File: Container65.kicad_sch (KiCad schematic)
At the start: 25 parts

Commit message: Matrix created
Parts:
- removed C? (x9): 100n, Capacitor_SMD:C_0603_1608Metric, symbol Device:C
- removed C? (x2): 1u, Capacitor_SMD:C_0603_1608Metric, symbol Device:C
- removed C? (x2): 10u, Capacitor_SMD:C_0603_1608Metric, symbol Device:C
- removed C? (x2): 15pf, Capacitor_SMD:C_0603_1608Metric, symbol Device:C
- removed J?: TYPE-C-31-M-12, Connector_USB:USB_C_Receptacle_HRO_TYPE-C-31-M-12, symbol Connector:USB_C_Receptacle_USB2.0
- removed J?: Conn_01x02, Connector_PinHeader_2.54mm:PinHeader_1x03_P2.54mm_Vertical, symbol Connector_Generic:Conn_01x03
- removed R? (x2): 5.1k, Resistor_SMD:R_0603_1608Metric, symbol Device:R
- removed R? (x2): 22, Resistor_SMD:R_0603_1608Metric, symbol Device:R
- removed R?: 1k, Resistor_SMD:R_0603_1608Metric, symbol Device:R
- removed U?: RP2040, RP2040_minimal:RP2040-QFN-56, symbol MCU_RaspberryPi_RP2040:RP2040
- removed U?: AP2112K-3.3, Package_TO_SOT_SMD:SOT-23-5, symbol Regulator_Linear:AP2112K-3.3
- removed Y?: Crystal_GND24_Small, Crystal:Crystal_SMD_3225-4Pin_3.2x2.5mm, symbol Device:Crystal_GND24_Small
- added C1, C2, C4, C5: 1uF, Capacitor_SMD:C_0402_1005Metric, symbol Device:C_Small
- added C10, C11, C12, C13, C14, C15, C16, C17, C8, C9: 100nF, Capacitor_SMD:C_0402_1005Metric, symbol Device:C_Small
- added C18, C3: 0.1 uF, Capacitor_SMD:C_0402_1005Metric, symbol Device:C_Small
- added C6, C7: 30pF, Capacitor_SMD:C_0402_1005Metric, symbol Device:C_Small
- added D1, D10, D11, D12, D13, D14, D15, D16, D17, D18, D19, D2, D20, D3, D4, D5, D6, D7, D8, D9: 1N4148W, Diode_SMD:D_SOD-123, symbol Diode:1N4148W
- added D21: Schottky 5819W, Diode_SMD:D_SOD-123, symbol Device:D_Schottky_Small
- added D22: Power LED (Blue), LED_SMD:LED_0805_2012Metric, symbol Device:LED_Small
- added F1: TLC_PSMD050, Fuse:Fuse_0805_2012Metric, symbol Device:Polyfuse_Small
- added FB1: 100@100MHz, Inductor_SMD:L_0805_2012Metric, symbol Device:FerriteBead_Small
- added J1: Conn_01x03, Connector_PinHeader_2.54mm:PinHeader_1x03_P2.54mm_Vertical, symbol Connector_Generic:Conn_01x03
- added J2: Conn_01x06, Connector_PinHeader_1.27mm:PinHeader_1x06_P1.27mm_Vertical, symbol Connector_Generic:Conn_01x06
- added MX-E-1, MX-E-2, MX-E-3, MX-E-4, MX-E-5, MX-E-6: MX-2U, MX_Only:MXOnly-1U-NoLEDHotswap, symbol MX_Alps_Hybrid:MX-NoLED
- added MX1, MX10, MX11, MX12, MX13, MX14, MX15, MX16, MX17, MX18, MX19, MX2, MX20, MX3, MX4, MX5, MX6, MX7, MX8, MX9: MX-1U, MX_Only:MXOnly-1U-NoLEDHotswap, symbol MX_Alps_Hybrid:MX-NoLED
- added POGO1: Conn_01x04, 65Numpad:PogoConnector, symbol Connector_Generic:Conn_01x04
- added POGO2: Conn_01x04, 65Numpad:PogoConnectorMirrored, symbol Connector_Generic:Conn_01x04
- added R1, R2: 27 ohm, Resistor_SMD:R_0603_1608Metric, symbol Device:R_Small
- added R3, R5: 1k ohm, Resistor_SMD:R_0402_1005Metric, symbol Device:R_Small
- added R4, R8: 10k ohm, Resistor_SMD:R_0402_1005Metric, symbol Device:R_Small
- added R6, R7: 5.1k, Resistor_SMD:R_0402_1005Metric, symbol Device:R_Small
- added R9: 1k5 ohm, Resistor_SMD:R_0402_1005Metric, symbol Device:R_Small
- added U1: RP2040, footprints:rp2040, symbol rp2040:RP2040
- added U2: TYPE-C-31-M-12, footprints:simple-usb-c, symbol simple-usb-c:TYPE-C-31-M-12
- added U3: XC6206PxxxMR, Package_TO_SOT_SMD:SOT-23, symbol Regulator_Linear:XC6206PxxxMR
- added U4: W25Q128JVS, Package_SO:SOIC-8_5.23x5.23mm_P1.27mm, symbol Memory_Flash:W25Q128JVS
- added U5: USB Boot, footprints:tactile-switch, symbol tactile-switch:TS-1187A-B-A-B
- added U6: Reset, footprints:tactile-switch, symbol tactile-switch:TS-1187A-B-A-B
- added Y1: 12MHz - 20pF, Crystal:Crystal_SMD_3225-4Pin_3.2x2.5mm, symbol Device:Crystal_GND24_Small
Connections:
- net +1V1: now also C16.1, C17.1, C2.1, U1.23 (DVDD), U1.45 (VREG_VOUT), U1.50 (DVDD)
- net +3V3: now also C1.1, C10.1, C11.1, C12.1, C13.1, C14.1, C15.1, C3.1, C5.1, C8.1, C9.1, R4.1, R8.2, R9.1, U1.1 (IOVDD), U1.10 (IOVDD), U1.22 (IOVDD), U1.33 (IOVDD), U1.42 (IOVDD), U1.43 (ADC_AVDD), U1.44 (VREG_IN), U1.48 (USB_VDD), U1.49 (IOVDD), U3.2 (VO), U4.8 (VCC)
- net +5V: now also C4.1, FB1.2, U3.3 (VI)
- net CS: now also J2.4 (Pin_4), U1.41 (GPIO29_ADC3)
- net GND: now also C1.2, C10.2, C11.2, C12.2, C13.2, C14.2, C15.2, C16.2, C17.2, C18.2, C2.2, C3.2, C4.2, C5.2, C6.2, C7.2, C8.2, C9.2, J1.3 (Pin_3), J2.5 (Pin_5), POGO1.1 (Pin_1), POGO2.1 (Pin_1), R6.2, R7.2, U1.19 (TESTEN), U1.57 (GND), U2.A1 (GND), U2.A12 (GND), U2.B1 (GND), U2.B12 (GND), U3.1 (GND), U4.4 (GND), U5.1 (A), U5.2 (B), U6.1 (A), U6.2 (B), Y1.2, Y1.4
- net MISO: now also J2.3 (Pin_3), U1.40 (GPIO28_ADC2)
- net MOSI: now also J2.2 (Pin_2), U1.39 (GPIO27_ADC1)
- net QSPI_SCLK: now also U1.52 (QSPI_SCLK), U4.6 (CLK)
- net QSPI_SD0: now also U1.53 (QSPI_SD0), U4.5 (DI(IO0))
- net QSPI_SD1: now also U1.55 (QSPI_SD1), U4.2 (DO(IO1))
- net QSPI_SD2: now also U1.54 (QSPI_SD2), U4.3 (IO2)
- net QSPI_SD3: now also U1.51 (QSPI_SD3), U4.7 (IO3)
- net QSPI_SS: now also R4.2, R5.1, U1.56 (QSPI_SS), U4.1 (~{CS})
- net SCK: now also J2.1 (Pin_1), U1.38 (GPIO26_ADC0)
- net SCL: now also POGO1.3 (Pin_3), POGO2.3 (Pin_3), U1.12 (GPIO9)
- net SDA: now also POGO1.2 (Pin_2), POGO2.2 (Pin_2), U1.11 (GPIO8)
- new net: D20.2 (A), MX-E-2.2 (ROW), MX20.2 (ROW)
- new net: D17.2 (A), MX-E-3.2 (ROW), MX17.2 (ROW)
- new net: D19.2 (A), MX-E-4.2 (ROW), MX19.2 (ROW)
- new net: D21.1 (K), F1.1
- new net: F1.2, FB1.1
- new net: D8.2 (A), MX-E-5.2 (ROW), MX8.2 (ROW)
- new net: D9.2 (A), MX9.2 (ROW)
- new net: D3.2 (A), MX3.2 (ROW)
- new net: D1.2 (A), MX1.2 (ROW)
- new net: D22.2 (A), R9.2
- new net: D18.2 (A), MX18.2 (ROW)
- new net: D16.2 (A), MX-E-6.2 (ROW), MX16.2 (ROW)
- new net: D10.2 (A), MX10.2 (ROW)
- new net: D11.2 (A), MX11.2 (ROW)
- new net: D2.2 (A), MX2.2 (ROW)
- new net: D13.2 (A), MX13.2 (ROW)
- new net: D6.2 (A), MX6.2 (ROW)
- new net: D4.2 (A), MX4.2 (ROW)
- new net: D12.2 (A), MX-E-1.2 (ROW), MX12.2 (ROW)
- new net: R5.2, U5.3 (C), U5.4 (D)
- new net: D15.2 (A), MX15.2 (ROW)
- new net: D7.2 (A), MX7.2 (ROW)
- new net: D14.2 (A), MX14.2 (ROW)
- new net: D5.2 (A), MX5.2 (ROW)
- new net CC1: R7.1, U2.A5 (CC1)
- new net CC2: R6.1, U2.B5 (CC2)
- new net CLM1: U1.27 (GPIO16)
- new net CLM10: U1.17 (GPIO14)
- new net CLM11: U1.31 (GPIO20)
- new net CLM12: U1.34 (GPIO22)
- new net CLM13: U1.35 (GPIO23)
- new net CLM2: U1.28 (GPIO17)
- new net CLM3: U1.29 (GPIO18)
- new net CLM5: U1.13 (GPIO10)
- new net CLM6: U1.30 (GPIO19)
- new net CLM7: U1.14 (GPIO11)
- new net CLM8: U1.15 (GPIO12)
- new net CLM9: U1.16 (GPIO13)
- new net COL0: MX-E-3.1 (COL), MX1.1 (COL), MX13.1 (COL), MX17.1 (COL), MX5.1 (COL), MX9.1 (COL)
- new net COL1: MX10.1 (COL), MX14.1 (COL), MX18.1 (COL), MX2.1 (COL), MX6.1 (COL)
- new net COL2: MX-E-4.1 (COL), MX11.1 (COL), MX15.1 (COL), MX19.1 (COL), MX3.1 (COL), MX7.1 (COL)
- new net COL3: MX-E-1.1 (COL), MX-E-2.1 (COL), MX-E-5.1 (COL), MX-E-6.1 (COL), MX12.1 (COL), MX16.1 (COL), MX20.1 (COL), MX4.1 (COL), MX8.1 (COL)
- new net OSC_IN: C7.1, R3.1, Y1.3
- new net OSC_OUT: C6.1, U1.20 (XIN), Y1.1
- new net ROW0: D1.1 (K), D2.1 (K), D3.1 (K), D4.1 (K)
- new net ROW1: D5.1 (K), D6.1 (K), D7.1 (K), D8.1 (K), U1.37 (GPIO25)
- new net ROW2: D10.1 (K), D11.1 (K), D12.1 (K), D9.1 (K)
- new net ROW3: D13.1 (K), D14.1 (K), D15.1 (K), D16.1 (K)
- new net ROW4: D17.1 (K), D18.1 (K), D19.1 (K), D20.1 (K), U1.18 (GPIO15)
- new net ROW5: U1.36 (GPIO24)
- new net RUN: C18.1, R8.1, U1.26 (RUN), U6.3 (C), U6.4 (D)
- new net SWCLK: J1.2 (Pin_2), U1.24 (SWCLK)
- new net SWD: J1.1 (Pin_1), U1.25 (SWD)
- new net USB+: R1.2, U2.A6 (DP1), U2.B6 (DP2)
- new net USB-: R2.2, U2.A7 (DN1), U2.B7 (DN2)
- new net USB_MCU+: R1.1, U1.47 (USB_DP)
- new net USB_MCU-: R2.1, U1.46 (USB_DM)
- new net USER_LED: D22.1 (K), U1.2 (GPIO0)
- new net VBUS: D21.2 (A), U2.A4 (VBUS), U2.A9 (VBUS), U2.B4 (VBUS), U2.B9 (VBUS)
- new net VCC: J2.6 (Pin_6), POGO1.4 (Pin_4), POGO2.4 (Pin_4)
- new net XOUT_MCU: R3.2, U1.21 (XOUT)
- no-connect marks 12 -> 14
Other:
- note added: "1uF caps near VREG_IN and VREG_OUT"
- note added: "Bypass Capacitors"
- note added: "Crystal Oscillator"
- note added: "QSPI Flash"
- note added: "Reset Circuit"
- note added: "Serial Wire Debug"
- note added: "USB + Voltage Regulator"
- note added: "USB Storage Boot Enable"
- note added: "User LED"
- note removed: "C16 must be close to Pin 44"
- note removed: "C6 must be close to Pin 45"
- note removed: "R2 and R3 must be close to RP2040"

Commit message: Design
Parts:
- removed POGO1: Conn_01x04, 65Numpad:PogoConnector, symbol Connector_Generic:Conn_01x04
- removed POGO2: Conn_01x04, 65Numpad:PogoConnectorMirrored, symbol Connector_Generic:Conn_01x04
- added POGO1: Conn_01x06_Male, extras:1x04_3.00mm_Magnetic Pogo_Male, symbol Connector:Conn_01x06_Male
- added POGO2: Conn_01x06_Female, extras:1x04_3.00mm_Magnetic Pogo_Female_2, symbol Connector:Conn_01x06_Female
- added U7: LEFT, Keebio-Parts:TRRS-PJ-320A, symbol keebio:TRRS
- added U8: RIGHT, Keebio-Parts:TRRS-PJ-320A, symbol keebio:TRRS
- C1, C10, C11, C12, C13, C14, C15, C16, C17, C18, C2, C3, C4, C5, C6, C7, C8, C9: footprint Capacitor_SMD:C_0402_1005Metric -> Keebio-Parts:C_0402
- D1, D10, D11, D12, D13, D14, D15, D16, D17, D18, D19, D2, D20, D21, D3, D4, D5, D6, D7, D8, D9: footprint Diode_SMD:D_SOD-123 -> Keebio-Parts:D_SOD123
- D22: footprint LED_SMD:LED_0805_2012Metric -> Keebio-Parts:R_0805
- F1: footprint Fuse:Fuse_0805_2012Metric -> Keebio-Parts:Fuse_0805
- MX-E-1, MX-E-2, MX-E-3, MX-E-4, MX-E-5, MX-E-6: footprint MX_Only:MXOnly-1U-NoLEDHotswap -> Switch_Keyboard_Hotswap_Kailh:SW_Hotswap_Kailh_MX_1.00u_Extras
- MX1, MX10, MX11, MX12, MX13, MX14, MX15, MX16, MX17, MX18, MX19, MX2, MX20, MX3, MX4, MX5, MX6, MX7, MX8, MX9: footprint MX_Only:MXOnly-1U-NoLEDHotswap -> Switch_Keyboard_Hotswap_Kailh:SW_Hotswap_Kailh_MX_1.00u_Modified
- R1, R2: footprint Resistor_SMD:R_0603_1608Metric -> Keebio-Parts:R_0402
- R3, R4, R5, R6, R7, R8, R9: footprint Resistor_SMD:R_0402_1005Metric -> Keebio-Parts:R_0402
- U1: footprint footprints:rp2040 -> extras:rp2040
- U2: footprint footprints:simple-usb-c -> extras:simple-usb-c
- U5, U6: footprint footprints:tactile-switch -> extras:tactile-switch
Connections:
- net GND: now also POGO1.1 (Pin_1), POGO1.5 (Pin_5), POGO1.6 (Pin_6), POGO2.1 (Pin_1), POGO2.5 (Pin_5), POGO2.6 (Pin_6)
- net SCL: now also POGO1.3 (Pin_3), POGO2.3 (Pin_3)
- net SDA: now also POGO1.2 (Pin_2), POGO2.2 (Pin_2)
- net VCC: now also POGO1.4 (Pin_4), POGO2.4 (Pin_4)

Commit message: Copy from backup
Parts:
- U7, U8: footprint Keebio-Parts:TRRS-PJ-320A -> Keebio-Parts:TRRS-PJ-320D
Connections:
- net GND: now also U7.3 (RING1), U8.3 (RING1)
- net SCL: now also U7.1 (SLEEVE), U8.1 (SLEEVE)
- net SDA: now also U7.4 (RING2), U8.4 (RING2)
- net VCC: now also U7.2 (TIP), U8.2 (TIP)
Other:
- moved on the sheet: U7, U8
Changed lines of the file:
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@@
+    )
+  )
+  (global_label "VCC" (shape input) (at 248.92 20.32 180)
+    (effects (font (size 1.27 1.27)) (justify right))
+    (property "Intersheet References" "${INTERSHEET_REFS}" (id 0) (at -158.75 -7.62 0)
+      (effects (font (size 1.27 1.27)) hide)
     )
   )
@@
     )
   )
+  (global_label "GND" (shape input) (at 222.25 22.86 180)
+    (effects (font (size 1.27 1.27)) (justify right))
+    (property "Intersheet References" "${INTERSHEET_REFS}" (id 0) (at -185.42 -2.54 0)
+      (effects (font (size 1.27 1.27)) hide)
+    )
+  )
   (global_label "XOUT_MCU" (shape input) (at 42.545 105.41 270) (fields_autoplaced)
     (effects (font (size 1.27 1.27)) (justify right))
@@
     )
   )
+  (global_label "SCL" (shape input) (at 222.25 27.94 180) (fields_autoplaced)
+    (effects (font (size 1.27 1.27)) (justify right))
+    (property "Intersheet References" "${INTERSHEET_REFS}" (id 0) (at 377.19 187.96 0)
+      (effects (font (size 1.27 1.27)) hide)
+    )
+  )
   (global_label "QSPI_SD3" (shape input) (at 50.8 77.47 180) (fields_autoplaced)
     (effects (font (size 1.27 1.27)) (justify right))
@@
     )
   )
+  (global_label "VCC" (shape input) (at 222.25 20.32 180)
+    (effects (font (size 1.27 1.27)) (justify right))
+    (property "Intersheet References" "${INTERSHEET_REFS}" (id 0) (at -185.42 -7.62 0)
+      (effects (font (size 1.27 1.27)) hide)
+    )
+  )
   (global_label "QSPI_SCLK" (shape input) (at 50.8 81.28 180) (fields_autoplaced)
     (effects (font (size 1.27 1.27)) (justify right))
@@
     )
   )
+  (global_label "SCL" (shape input) (at 248.92 27.94 180) (fields_autoplaced)
+    (effects (font (size 1.27 1.27)) (justify right))
+    (property "Intersheet References" "${INTERSHEET_REFS}" (id 0) (at 403.86 187.96 0)
+      (effects (font (size 1.27 1.27)) hide)
+    )
+  )
   (global_label "CLM1" (shape input) (at 114.3 105.41 0) (fields_autoplaced)
     (effects (font (size 1.27 1.27)) (justify left))
@@
     )
   )
+  (global_label "SDA" (shape input) (at 222.25 25.4 180) (fields_autoplaced)
+    (effects (font (size 1.27 1.27)) (justify right))
+    (property "Intersheet References" "${INTERSHEET_REFS}" (id 0) (at 377.19 182.88 0)
+      (effects (font (size 1.27 1.27)) hide)
+    )
+  )
   (global_label "QSPI_SS" (shape input) (at 178.435 217.17 180) (fields_autoplaced)
     (effects (font (size 1.27 1.27)) (justify right))
@@
     )
   )
+  (global_label "GND" (shape input) (at 248.92 22.86 180)
+    (effects (font (size 1.27 1.27)) (justify right))
+    (property "Intersheet References" "${INTERSHEET_REFS}" (id 0) (at -158.75 -2.54 0)
+      (effects (font (size 1.27 1.27)) hide)
+    )
+  )
   (global_label "CC1" (shape input) (at 52.705 207.01 0) (fields_autoplaced)
     (effects (font (size 1.27 1.27)) (justify left))
@@
     (property "Intersheet References" "${INTERSHEET_REFS}" (id 0) (at 121.6721 95.3294 0)
       (effects (font (size 1.27 1.27)) (justify left) hide)
+    )
+  )
+  (global_label "SDA" (shape input) (at 248.92 25.4 180) (fields_autoplaced)
+    (effects (font (size 1.27 1.27)) (justify right))
+    (property "Intersheet References" "${INTERSHEET_REFS}" (id 0) (at 403.86 182.88 0)
+      (effects (font (size 1.27 1.27)) hide)
     )
   )
@@
     (pin "2")
   )
-  (symbol (lib_id "keebio:TRRS") (at 226.06 30.48 0) (unit 1)
-    (in_bom yes) (on_board yes) (fields_autoplaced)
-    (property "Reference" "U7" (id 0) (at 232.41 22.86 0)
+  (symbol (lib_id "keebio:TRRS") (at 231.14 30.48 0) (unit 1)
+    (in_bom yes) (on_board yes) (fields_autoplaced)
+    (property "Reference" "U7" (id 0) (at 237.49 22.86 0)
       (effects (font (size 1.524 1.524)) (justify left))
     )
-    (property "Value" "LEFT" (id 1) (at 232.41 26.67 0)
+    (property "Value" "LEFT" (id 1) (at 237.49 26.67 0)
       (effects (font (size 1.524 1.524)) (justify left))
     )
-    (property "Footprint" "Keebio-Parts:TRRS-PJ-320A" (id 2) (at 229.87 30.48 0)
-      (effects (font (size 1.524 1.524)) hide)
-    )
-    (property "Datasheet" "" (id 3) (at 229.87 30.48 0)
+    (property "Footprint" "Keebio-Parts:TRRS-PJ-320D" (id 2) (at 234.95 30.48 0)
+      (effects (font (size 1.524 1.524)) hide)
+    )
+    (property "Datasheet" "" (id 3) (at 234.95 30.48 0)
       (effects (font (size 1.524 1.524)) hide)
     )
@@
     (pin "2")
   )
-  (symbol (lib_id "keebio:TRRS") (at 250.19 30.48 0) (unit 1)
-    (in_bom yes) (on_board yes) (fields_autoplaced)
-    (property "Reference" "U8" (id 0) (at 256.54 22.86 0)
+  (symbol (lib_id "keebio:TRRS") (at 257.81 30.48 0) (unit 1)
+    (in_bom yes) (on_board yes) (fields_autoplaced)
+    (property "Reference" "U8" (id 0) (at 264.16 22.86 0)
       (effects (font (size 1.524 1.524)) (justify left))
     )
-    (property "Value" "RIGHT" (id 1) (at 256.54 26.67 0)
+    (property "Value" "RIGHT" (id 1) (at 264.16 26.67 0)
       (effects (font (size 1.524 1.524)) (justify left))
     )
-    (property "Footprint" "Keebio-Parts:TRRS-PJ-320A" (id 2) (at 254 30.48 0)
-      (effects (font (size 1.524 1.524)) hide)
-    )
-    (property "Datasheet" "" (id 3) (at 254 30.48 0)
+    (property "Footprint" "Keebio-Parts:TRRS-PJ-320D" (id 2) (at 261.62 30.48 0)
+      (effects (font (size 1.524 1.524)) hide)
+    )
+    (property "Datasheet" "" (id 3) (at 261.62 30.48 0)
       (effects (font (size 1.524 1.524)) hide)
     )
@@
     )
     (path "/98c150b7-049e-4fac-8f45-60f2576a64f5"
-      (reference "U7") (unit 1) (value "LEFT") (footprint "Keebio-Parts:TRRS-PJ-320A")
+      (reference "U7") (unit 1) (value "LEFT") (footprint "Keebio-Parts:TRRS-PJ-320D")
     )
     (path "/bc53684d-e6be-49c8-ab37-fbed73b271a0"
-      (reference "U8") (unit 1) (value "RIGHT") (footprint "Keebio-Parts:TRRS-PJ-320A")
+      (reference "U8") (unit 1) (value "RIGHT") (footprint "Keebio-Parts:TRRS-PJ-320D")
     )
     (path "/3d1b2c07-f701-4a6d-98db-4deeb93d797f"

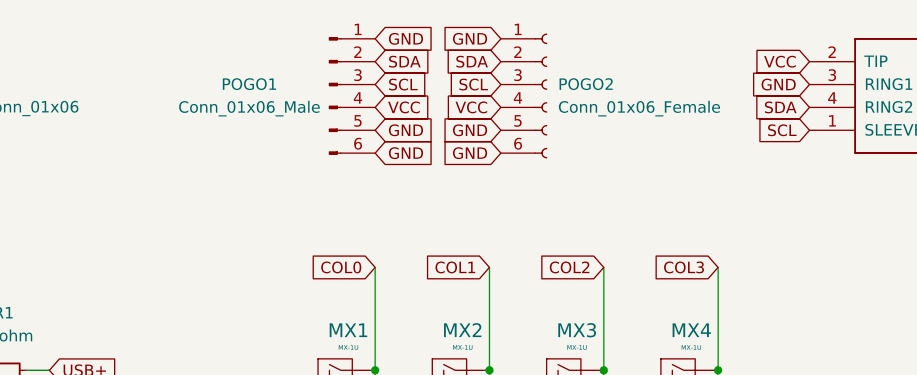
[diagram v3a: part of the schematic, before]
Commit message: Added OLED
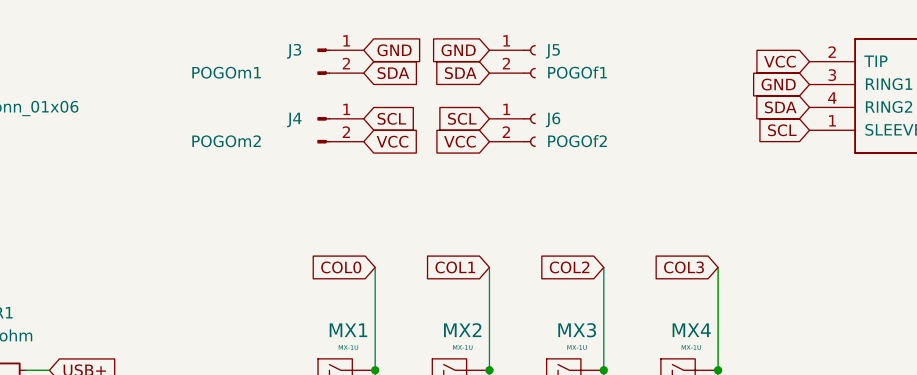
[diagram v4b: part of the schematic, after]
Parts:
- removed POGO1: Conn_01x06_Male, extras:1x04_3.00mm_Magnetic Pogo_Male, symbol Connector:Conn_01x06_Male
- removed POGO2: Conn_01x06_Female, extras:1x04_3.00mm_Magnetic Pogo_Female_2, symbol Connector:Conn_01x06_Female
- added J3: POGOm1, extras:1x02_2.54_Pogo Male GND, symbol Connector:Conn_01x02_Male
- added J4: POGOm2, extras:1x02_2.54_Pogo Male, symbol Connector:Conn_01x02_Male
- added J5: POGOf1, extras:1x02_2.54_Pogo Female GND, symbol Connector:Conn_01x02_Female
- added J6: POGOf2, extras:1x02_2.54_Pogo Female, symbol Connector:Conn_01x02_Female
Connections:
- net GND: now also J3.1 (Pin_1), J5.1 (Pin_1)
- net SCL: now also J4.1 (Pin_1), J6.1 (Pin_1)
- net SDA: now also J3.2 (Pin_2), J5.2 (Pin_2)
- net VCC: now also J4.2 (Pin_2), J6.2 (Pin_2)
